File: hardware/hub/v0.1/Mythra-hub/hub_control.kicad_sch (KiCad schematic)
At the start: 10 parts, among them U1 TUSB8042A, Y1 24MHz

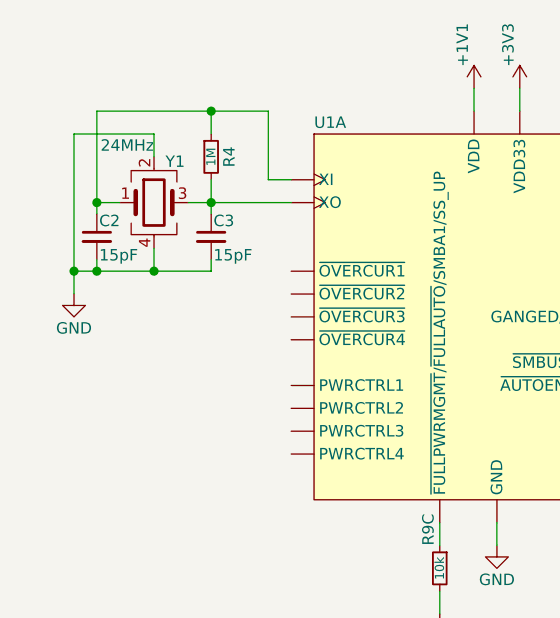
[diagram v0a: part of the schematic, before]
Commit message: Re-jigged the hierachy and performed some cleanup
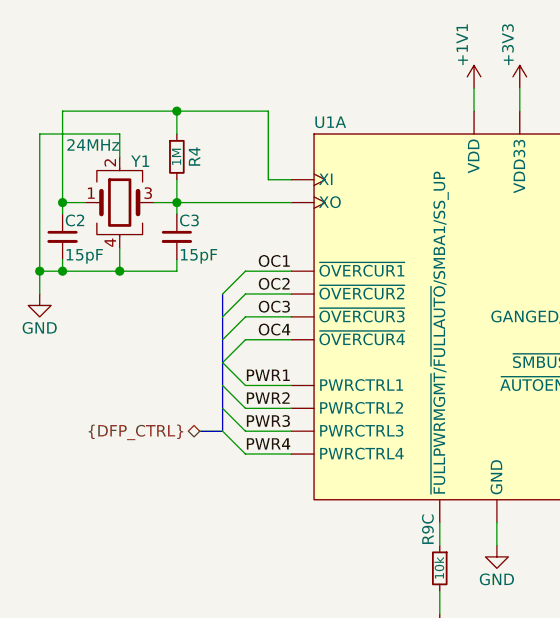
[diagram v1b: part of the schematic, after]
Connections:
- net PWR4: now reaches U1.32 (PWRCTRL4)
- net PWR3: now reaches U1.33 (PWRCTRL3)
- net PWR2: now reaches U1.35 (PWRCTRL2)
- net PWR1: now reaches U1.36 (PWRCTRL1)
- net OC4: now reaches U1.43 (~{OVERCUR4})
- net OC3: now reaches U1.44 (~{OVERCUR3})
- net OC1: now reaches U1.46 (~{OVERCUR1})
- net OC2: now reaches U1.47 (~{OVERCUR2})
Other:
- moved on the sheet: C2, C3, R4, Y1

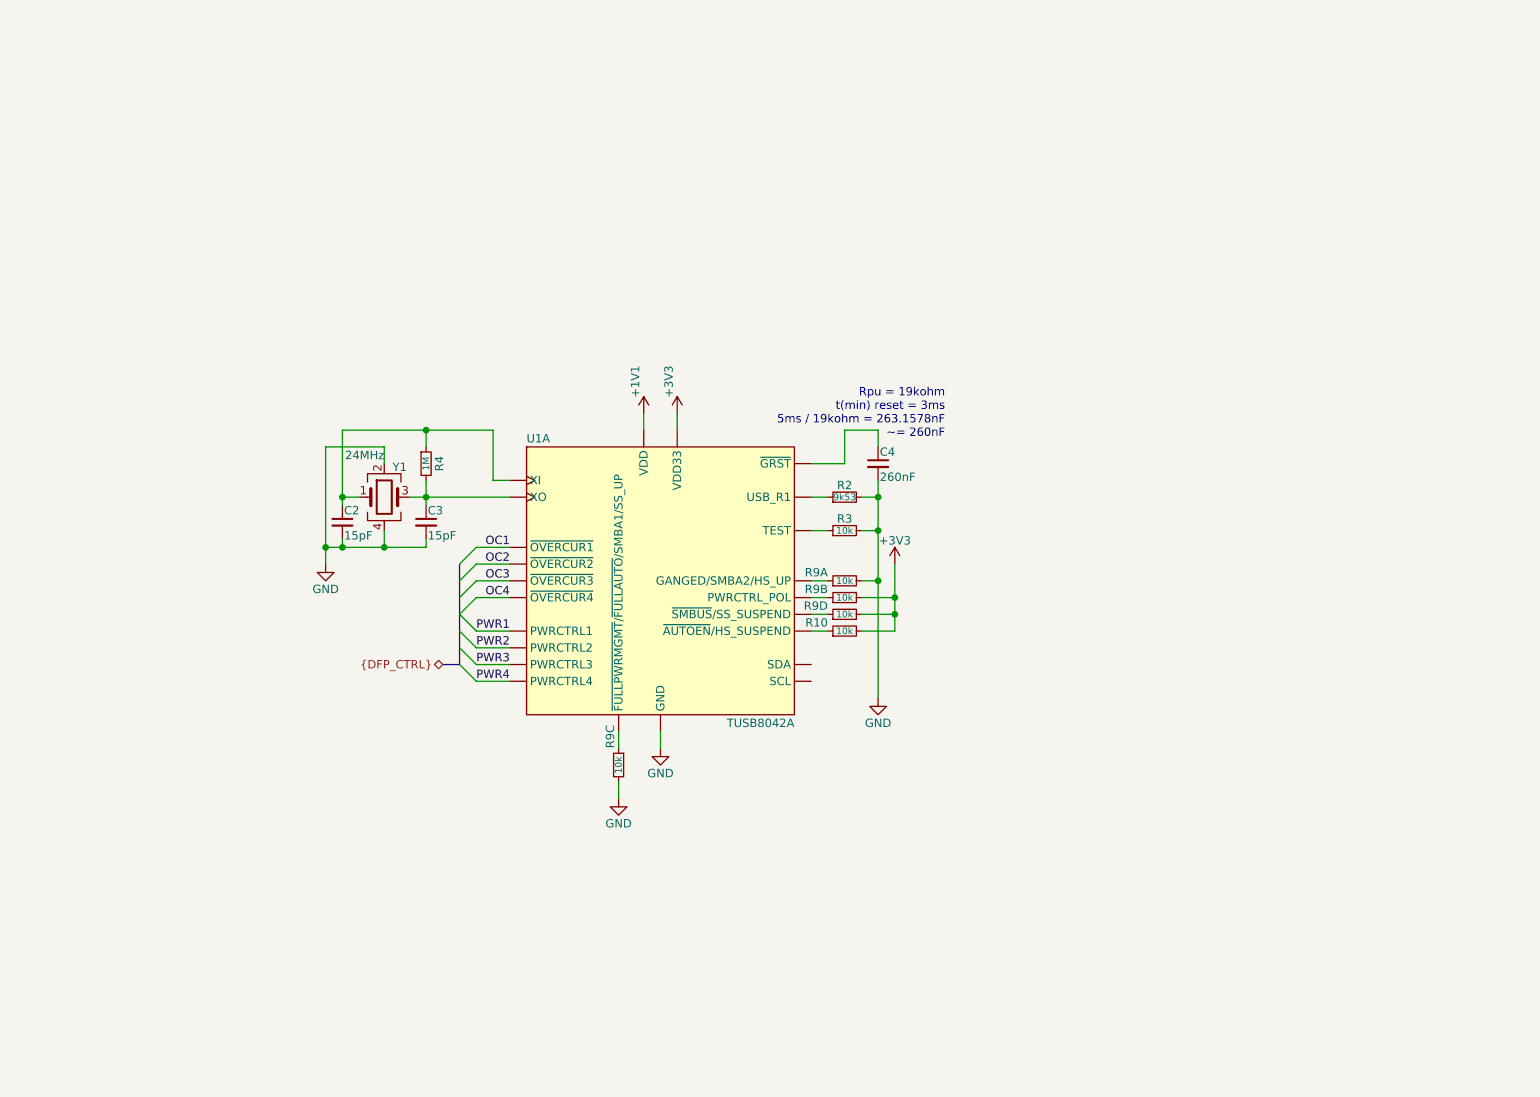
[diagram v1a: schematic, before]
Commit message: Created the DC-DC supply for the hub's core 1.1V rail and added the DFP Type-C recepticals and their shield components
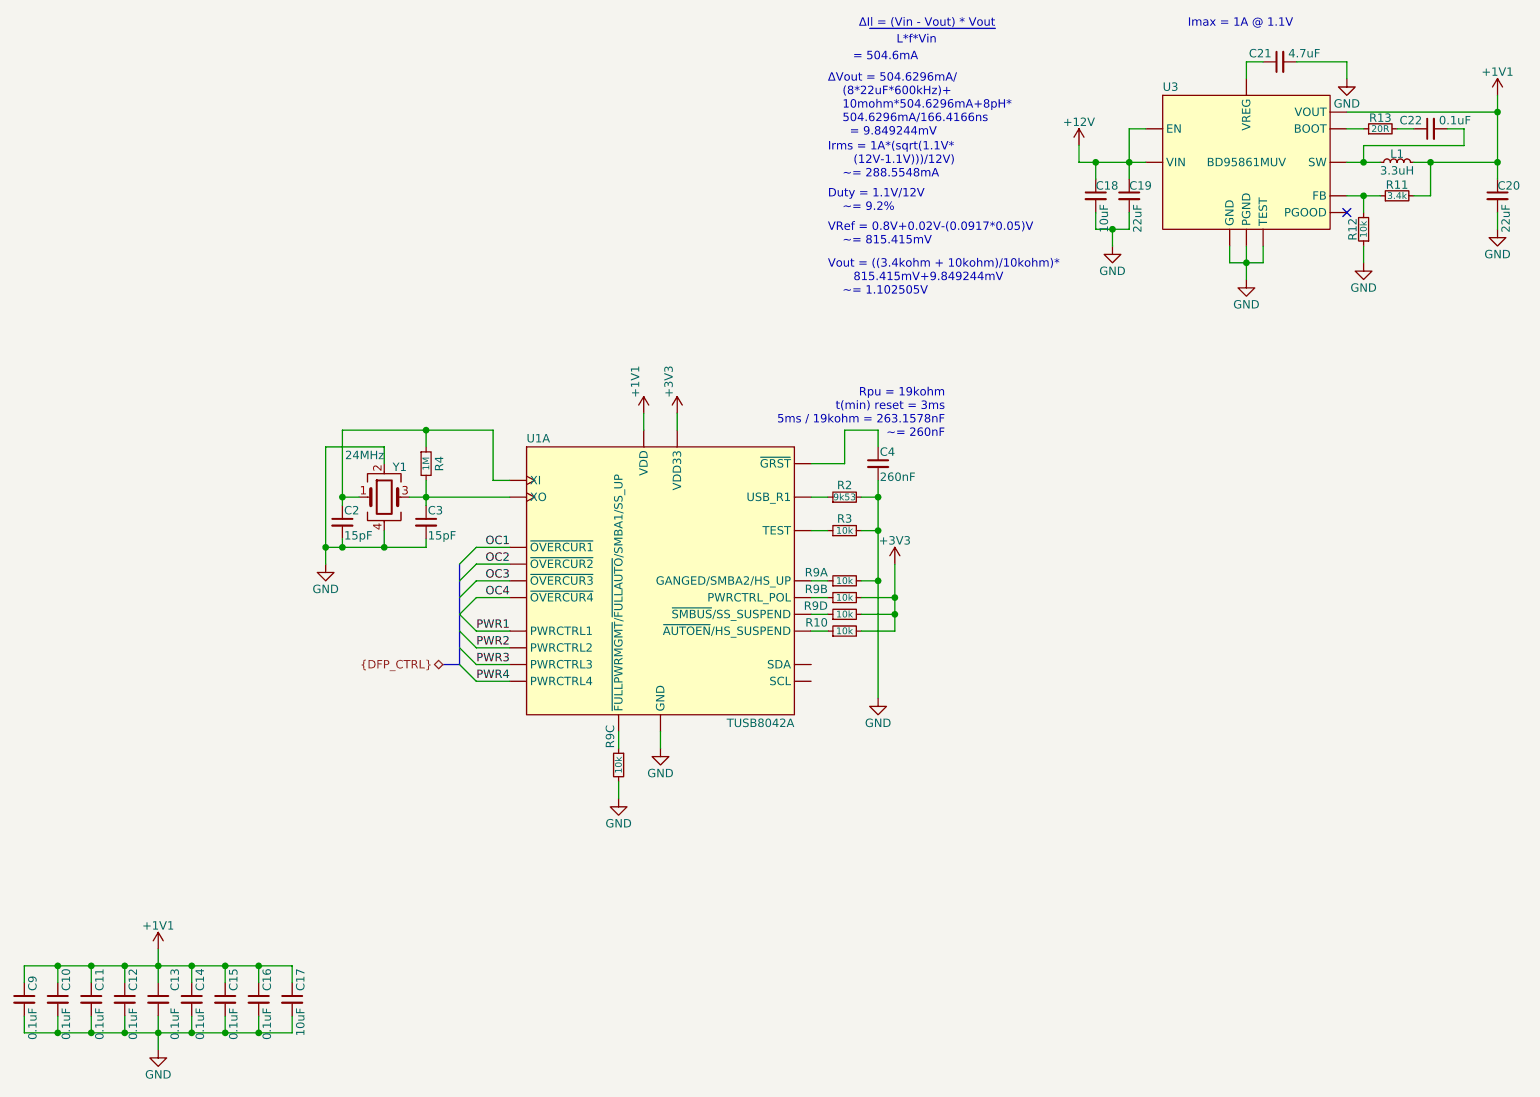
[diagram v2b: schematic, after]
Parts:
- added C10, C11, C12, C13, C14, C15, C16, C22, C9: 0.1uF, rhais_rcl:C0402, symbol Device:C_Small
- added C17, C18: 10uF, rhais_rcl:C0603, symbol Device:C_Small
- added C19: 22uF, rhais_rcl:C1206, symbol Device:C_Small
- added C20: 22uF, rhais_rcl:C0603, symbol Device:C_Small
- added C21: 4.7uF, rhais_rcl:C0402, symbol Device:C_Small
- added L1: 3.3uH, rhais_coilcraft:XAL40xx, symbol Device:L_Small
- added R11: 3.4k, rhais_rcl:R0402, symbol Device:R_Small
- added R12: 10k, rhais_rcl:R0402, symbol Device:R_Small
- added R13: 20R, rhais_rcl:R0402, symbol Device:R_Small
- added U3: BD95861MUV, rhais_package-qfn:VQFN-24-1EP_4x4mm_P0.5mm_EP2x2mm, symbol DX-MON:BD95861MUV
- C2, C3: MFR (none) -> Yageo; MPN (none) -> CC0402JRNPO9BN150; OC_FARNELL (none) -> 3019172; OC_LCSC (none) -> C106997; URL_FARNELL (none) -> https://uk.farnell.com/yageo/cc0402jrnpo9bn150/cap-15pf-50v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; URL_LCSC (none) -> https://lcsc.com/product-detail/Multilayer-Ceramic-Capacito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
- C4: MFR (none) -> Yageo; MPN (none) -> CC0402KRX5R6BB224; OC_FARNELL (none) -> 9402055; OC_LCSC (none) -> C106257; URL_FARNELL (none) -> https://uk.farnell.com/yageo/cc0402krx5r6bb224/cap-0-22-f-1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; URL_LCSC (none) -> https://lcsc.com/product-detail/Multilayer-Ceramic-Capacito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
- R10, R3: footprint rhais_rcl:C0402 -> rhais_rcl:R0402; MFR (none) -> Yageo; MPN (none) -> RC0402FR-0710KL; OC_LCSC (none) -> C60490; URL_LCSC (none) -> https://lcsc.com/product-detail/Chip-Resistor-Surface-Mount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
- R2: MFR (none) -> Multicomp Pro; MPN (none) -> MCMR04X9531FTL; OC_FARNELL (none) -> 2073325; URL_FARNELL (none) -> https://uk.farnell.com/multicomp/mcmr04x9531ftl/res-9k53-1-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
- R4: MFR (none) -> Multicomp Pro; MPN (none) -> MCWR04X1004FTL; OC_FARNELL (none) -> 2447127; URL_FARNELL (none) -> https://uk.farnell.com/multicomp/mcwr04x1004ftl/res-1m-1-0-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
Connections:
- net +1V1: now also C10.1, C11.1, C12.1, C13.1, C14.1, C15.1, C16.1, C17.1, C20.1, C9.1, L1.2, R11.2, U3.19 (VOUT)
- net GND: now also C10.2, C11.2, C12.2, C13.2, C14.2, C15.2, C16.2, C17.2, C18.2, C19.2, C20.2, C21.2, C9.2, R12.1, U3.21 (GND), U3.23 (TEST), U3.25 (GND), U3.5 (PGND), U3.6 (PGND), U3.7 (PGND), U3.8 (PGND), U3.9 (PGND)
- new net: C22.1, R13.2
- new net: C22.2, L1.1, U3.10 (SW), U3.11 (SW), U3.12 (SW), U3.13 (SW), U3.14 (SW), U3.15 (SW)
- new net: R13.1, U3.16 (BOOT)
- new net: R11.1, R12.2, U3.20 (FB)
- new net: C21.1, U3.22 (VREG)
- new net +12V: C18.1, C19.1, U3.1 (VIN), U3.17 (EN), U3.2 (VIN), U3.24 (VIN), U3.3 (VIN), U3.4 (VIN)
- no-connect marks 0 -> 1
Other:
- note added: "= 504.6mA"
- note added: "Duty = 1.1V/12V ~= 9.2%"
- note added: "Imax = 1A @ 1.1V"
- note added: "Irms = 1A*(sqrt(1.1V* (12V-1.1V)))/12V) ~= 288.5548mA"
- note added: "L*f*Vin"
- note added: "VRef = 0.8V+0.02V-(0.0917*0.05)V ~= 815.415mV"
- note added: "Vout = ((3.4kohm + 10kohm)/10kohm)* 815.415mV+9.849244mV ~= 1.102505V"
- note added: "ΔIl = (Vin - Vout) * Vout"
- note added: "ΔVout = 504.6296mA/ (8*22uF*600kHz)+ 10mohm*504.6296mA+8pH* 504.6296mA/166.4166ns = 9.849244mV"
